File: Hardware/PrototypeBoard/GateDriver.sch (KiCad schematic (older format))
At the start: 38 parts, among them U8 TLE7185-1E

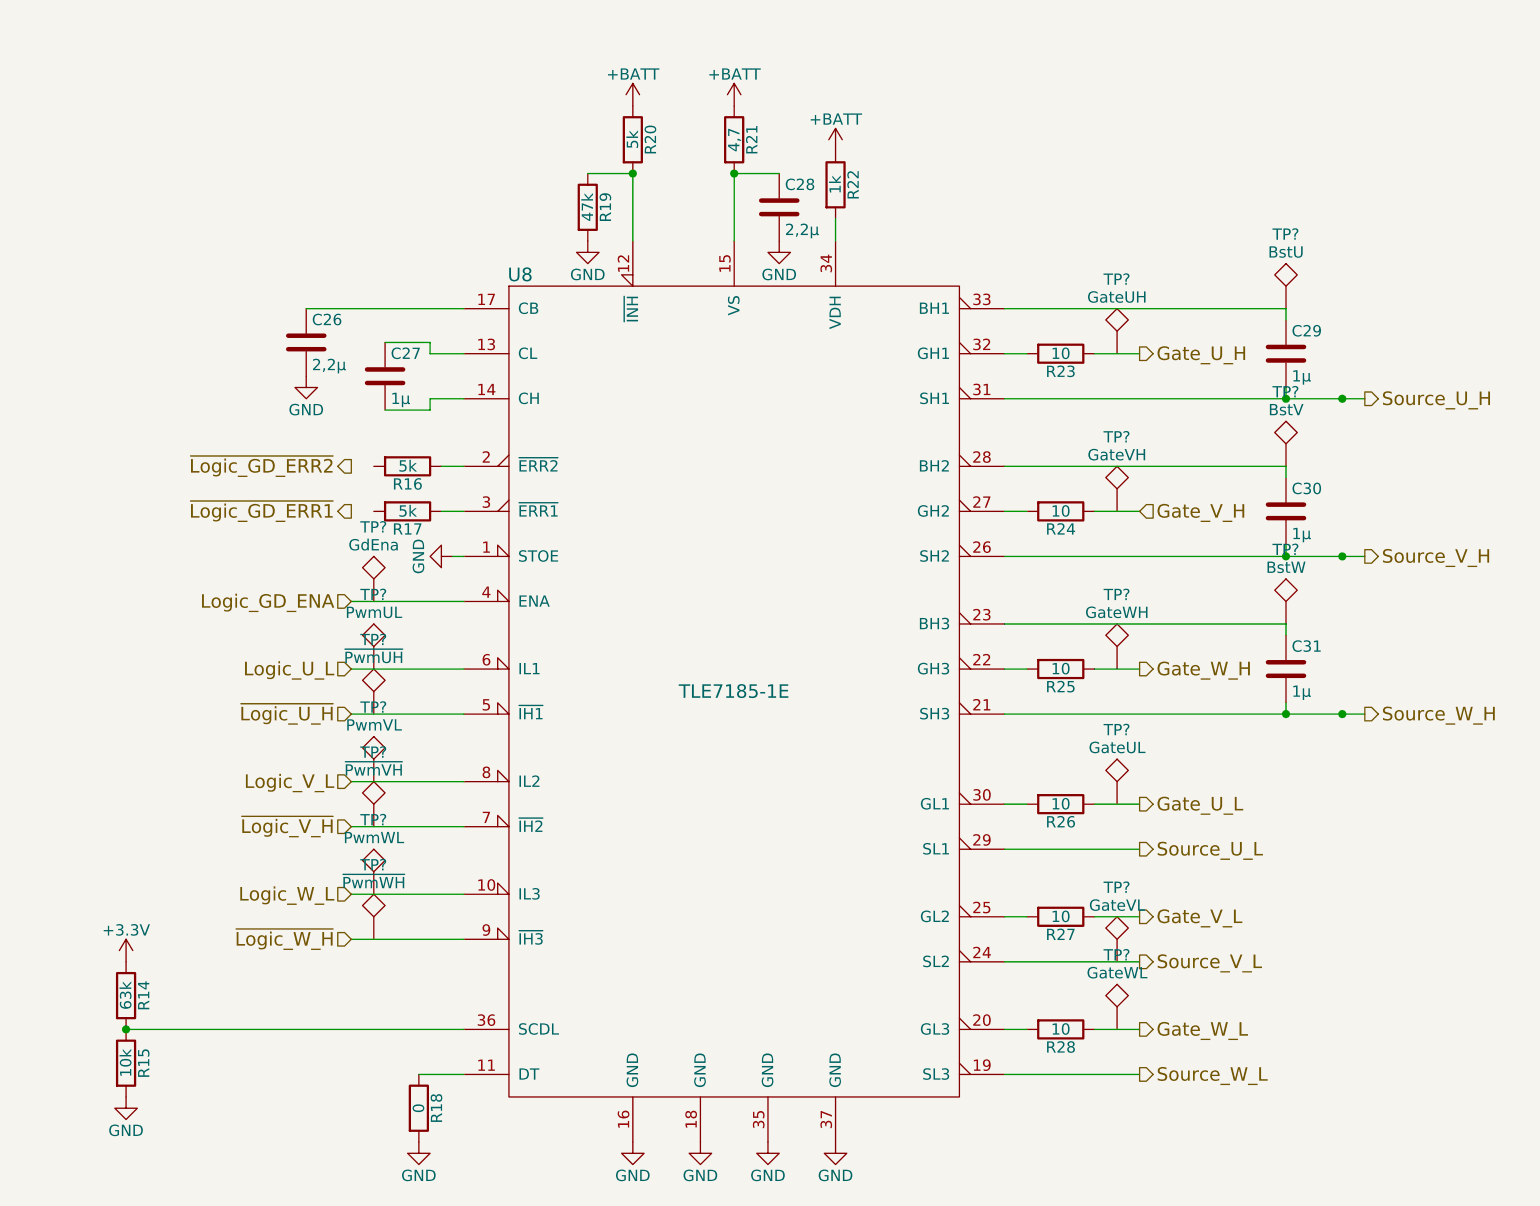
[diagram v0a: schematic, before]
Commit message: Fixed all ERC errors. Added power consumption estimation and other comments. Added links to datasheets. Dimensioned low pass and voltage dividers. Added TVS diodes for protection of voltage rails and ADC inputs. Added fuses. Added Testpoints. Added DC-link capacitors.
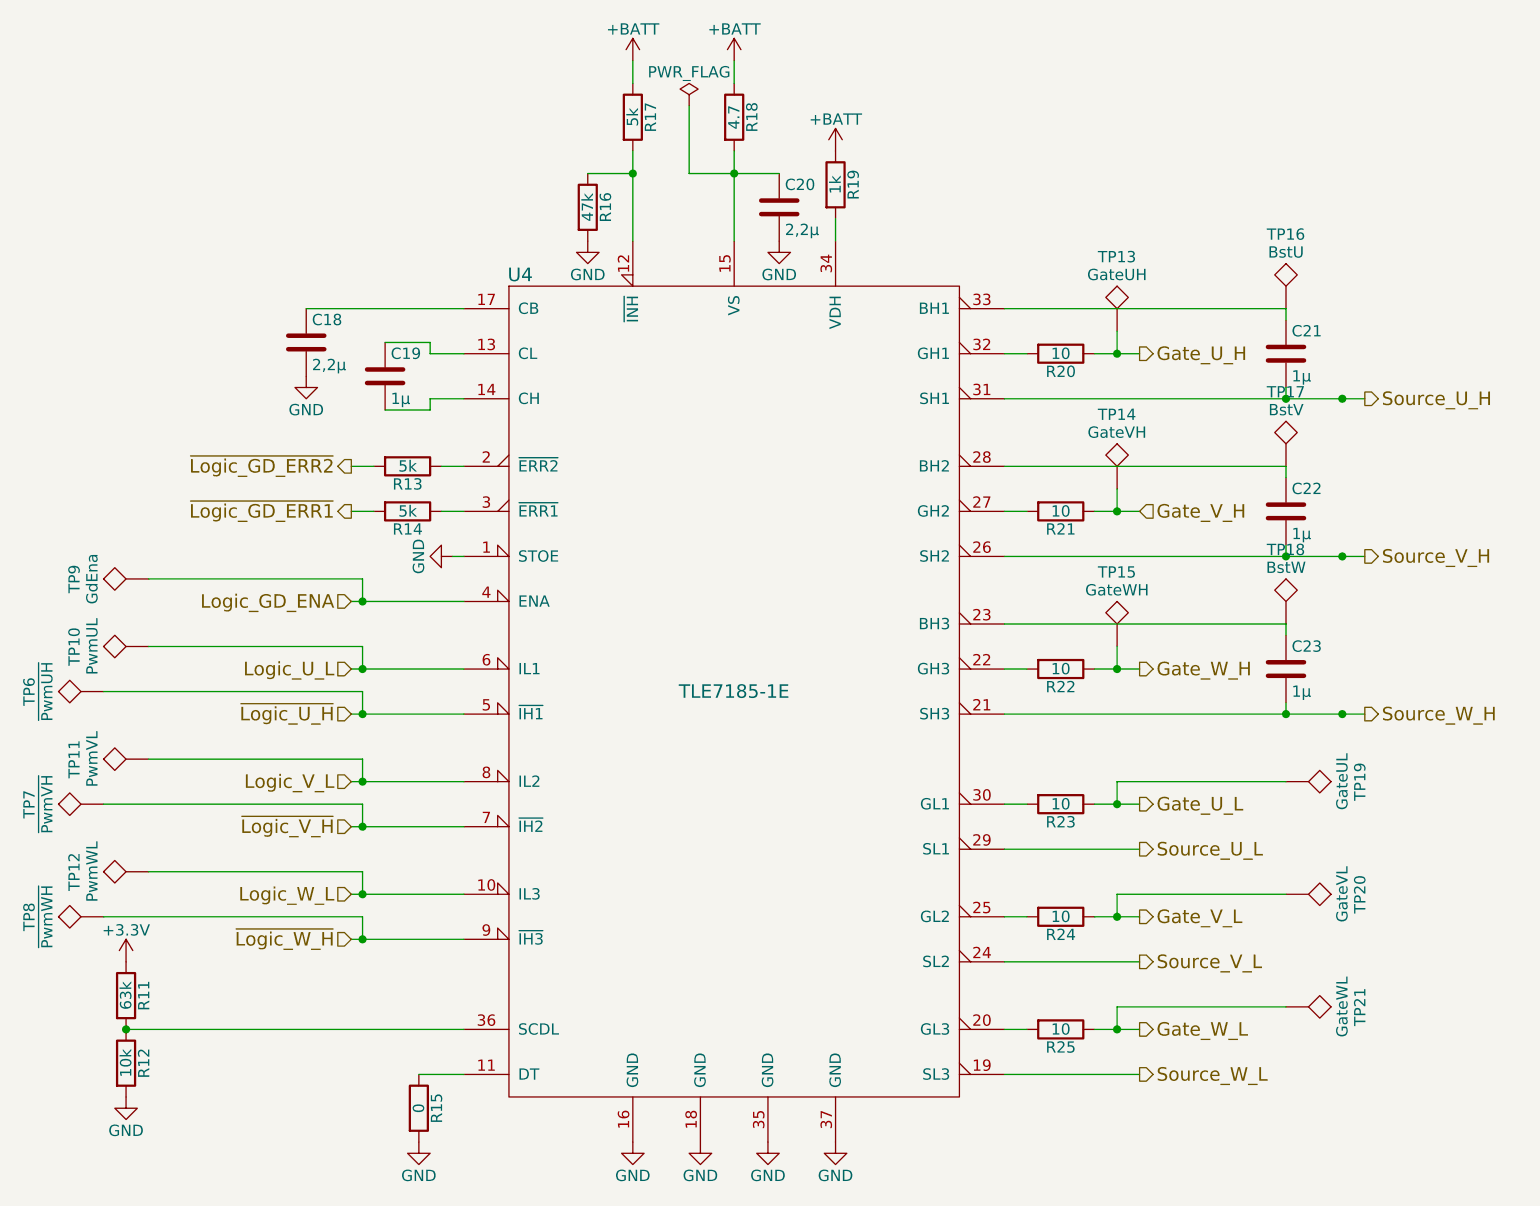
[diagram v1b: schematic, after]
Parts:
- R18: renamed from R21; value 4,7 -> 4.7
- gave numbers to parts that had none: 16
- renumbered C26 to C18, C27 to C19, C28 to C20, C29 to C21, C30 to C22, C31 to C23, R14 to R11, R15 to R12, R16 to R13, R17 to R14, R18 to R15, R19 to R16, R20 to R17, R22 to R19, R23 to R20, R24 to R21, R25 to R22, R26 to R23, R27 to R24, R28 to R25, U8 to U4
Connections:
- net Gate_U_H: now also TP13.1
- net Gate_U_L: now also TP19.1
- net Gate_V_H: now also TP14.1
- net Gate_V_L: now also TP20.1
- net Gate_W_H: now also TP15.1
- net Gate_W_L: now also TP21.1
- net Logic_GD_ENA: now also TP9.1
- net Logic_U_L: now also TP10.1
- net Logic_V_L: now also TP11.1
- net Logic_W_L: now also TP12.1
- net ~Logic_GD_ERR1: now also R14.2
- net ~Logic_GD_ERR2: now also R13.2
- net ~Logic_U_H: now also TP6.1
- net ~Logic_V_H: now also TP7.1
- net ~Logic_W_H: now also TP8.1
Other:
- moved on the sheet: R17, R18, TP10, TP11, TP12, TP13, TP14, TP15, TP19, TP20, TP21, TP6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

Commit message: forgot files
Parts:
- TP10, TP11, TP12, TP13, TP14, TP15, TP16, TP17, TP18, TP19, TP20, TP21, TP6, TP7, TP8, TP9: footprint (none) -> Measurement_Points:Measurement_Point_Round-TH_Big
- U4: footprint (none) -> libs:PG-DSO-36-38
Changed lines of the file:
@@
 F 0 "U4" H 3550 5450 60  0000 C CNN
 F 1 "TLE7185-1E" H 4500 3600 60  0000 C CNN
-F 2 "" H 4500 3600 60  0001 C CNN
+F 2 "libs:PG-DSO-36-38" H 4500 3600 60  0001 C CNN
 F 3 "" H 4500 3600 60  0000 C CNN
 	1    4500 3600
@@
 F 0 "TP17" H 6950 2900 50  0000 C BNN
 F 1 "BstV" H 6950 2850 50  0000 C CNN
-F 2 "" H 6950 2600 50  0001 C CNN
+F 2 "Measurement_Points:Measurement_Point_Round-TH_Big" H 6950 2600 50  0001 C CNN
 F 3 "" H 6950 2600 50  0001 C CNN
 	1    6950 2600
@@
 F 0 "TP16" H 6950 2200 50  0000 C BNN
 F 1 "BstU" H 6950 2150 50  0000 C CNN
-F 2 "" H 6950 1900 50  0001 C CNN
+F 2 "Measurement_Points:Measurement_Point_Round-TH_Big" H 6950 1900 50  0001 C CNN
 F 3 "" H 6950 1900 50  0001 C CNN
 	1    6950 1900
@@
 F 0 "TP18" H 6950 3600 50  0000 C BNN
 F 1 "BstW" H 6950 3550 50  0000 C CNN
-F 2 "" H 6950 3300 50  0001 C CNN
+F 2 "Measurement_Points:Measurement_Point_Round-TH_Big" H 6950 3300 50  0001 C CNN
 F 3 "" H 6950 3300 50  0001 C CNN
 	1    6950 3300
@@
 F 0 "TP14" H 6200 3000 50  0000 C BNN
 F 1 "GateVH" H 6200 2950 50  0000 C CNN
-F 2 "" H 6200 2700 50  0001 C CNN
+F 2 "Measurement_Points:Measurement_Point_Round-TH_Big" H 6200 2700 50  0001 C CNN
 F 3 "" H 6200 2700 50  0001 C CNN
 	1    6200 2700
@@
 F 0 "TP13" H 6200 2300 50  0000 C BNN
 F 1 "GateUH" H 6200 2250 50  0000 C CNN
-F 2 "" H 6200 2000 50  0001 C CNN
+F 2 "Measurement_Points:Measurement_Point_Round-TH_Big" H 6200 2000 50  0001 C CNN
 F 3 "" H 6200 2000 50  0001 C CNN
 	1    6200 2000
@@
 F 0 "TP15" H 6200 3700 50  0000 C BNN
 F 1 "GateWH" H 6200 3650 50  0000 C CNN
-F 2 "" H 6200 3400 50  0001 C CNN
+F 2 "Measurement_Points:Measurement_Point_Round-TH_Big" H 6200 3400 50  0001 C CNN
 F 3 "" H 6200 3400 50  0001 C CNN
 	1    6200 3400
@@
 F 0 "TP19" H 6950 4300 50  0000 C BNN
 F 1 "GateUL" H 6950 4250 50  0000 C CNN
-F 2 "" H 6950 4000 50  0001 C CNN
+F 2 "Measurement_Points:Measurement_Point_Round-TH_Big" H 6950 4000 50  0001 C CNN
 F 3 "" H 6950 4000 50  0001 C CNN
 	1    6950 4000
@@
 F 0 "TP20" H 6950 4800 50  0000 C BNN
 F 1 "GateVL" H 6950 4750 50  0000 C CNN
-F 2 "" H 6950 4500 50  0001 C CNN
+F 2 "Measurement_Points:Measurement_Point_Round-TH_Big" H 6950 4500 50  0001 C CNN
 F 3 "" H 6950 4500 50  0001 C CNN
 	1    6950 4500
@@
 F 0 "TP21" H 6950 5300 50  0000 C BNN
 F 1 "GateWL" H 6950 5250 50  0000 C CNN
-F 2 "" H 6950 5000 50  0001 C CNN
+F 2 "Measurement_Points:Measurement_Point_Round-TH_Big" H 6950 5000 50  0001 C CNN
 F 3 "" H 6950 5000 50  0001 C CNN
 	1    6950 5000
@@
 F 0 "TP9" H 1900 3400 50  0000 C BNN
 F 1 "GdEna" H 1900 3350 50  0000 C CNN
-F 2 "" H 1900 3100 50  0001 C CNN
+F 2 "Measurement_Points:Measurement_Point_Round-TH_Big" H 1900 3100 50  0001 C CNN
 F 3 "" H 1900 3100 50  0001 C CNN
 	1    1900 3100
@@
 F 0 "TP10" H 1900 3700 50  0000 C BNN
 F 1 "PwmUL" H 1900 3650 50  0000 C CNN
-F 2 "" H 1900 3400 50  0001 C CNN
+F 2 "Measurement_Points:Measurement_Point_Round-TH_Big" H 1900 3400 50  0001 C CNN
 F 3 "" H 1900 3400 50  0001 C CNN
 	1    1900 3400
@@
 F 0 "TP6" H 1700 3900 50  0000 C BNN
 F 1 "~PwmUH" H 1700 3850 50  0000 C CNN
-F 2 "" H 1700 3600 50  0001 C CNN
+F 2 "Measurement_Points:Measurement_Point_Round-TH_Big" H 1700 3600 50  0001 C CNN
 F 3 "" H 1700 3600 50  0001 C CNN
 	1    1700 3600
@@
 F 0 "TP11" H 1900 4200 50  0000 C BNN
 F 1 "PwmVL" H 1900 4150 50  0000 C CNN
-F 2 "" H 1900 3900 50  0001 C CNN
+F 2 "Measurement_Points:Measurement_Point_Round-TH_Big" H 1900 3900 50  0001 C CNN
 F 3 "" H 1900 3900 50  0001 C CNN
 	1    1900 3900
@@
 F 0 "TP7" H 1700 4400 50  0000 C BNN
 F 1 "~PwmVH" H 1700 4350 50  0000 C CNN
-F 2 "" H 1700 4100 50  0001 C CNN
+F 2 "Measurement_Points:Measurement_Point_Round-TH_Big" H 1700 4100 50  0001 C CNN
 F 3 "" H 1700 4100 50  0001 C CNN
 	1    1700 4100
@@
 F 0 "TP12" H 1900 4700 50  0000 C BNN
 F 1 "PwmWL" H 1900 4650 50  0000 C CNN
-F 2 "" H 1900 4400 50  0001 C CNN
+F 2 "Measurement_Points:Measurement_Point_Round-TH_Big" H 1900 4400 50  0001 C CNN
 F 3 "" H 1900 4400 50  0001 C CNN
 	1    1900 4400
@@
 F 0 "TP8" H 1700 4900 50  0000 C BNN
 F 1 "~PwmWH" H 1700 4850 50  0000 C CNN
-F 2 "" H 1700 4600 50  0001 C CNN
+F 2 "Measurement_Points:Measurement_Point_Round-TH_Big" H 1700 4600 50  0001 C CNN
 F 3 "" H 1700 4600 50  0001 C CNN
 	1    1700 4600

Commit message: minor progress in layout
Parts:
- TP10, TP11, TP12, TP13, TP14, TP15, TP16, TP17, TP18, TP19, TP20, TP21, TP6, TP7, TP8, TP9: footprint Measurement_Points:Measurement_Point_Round-TH_Big -> Measurement_Points:Measurement_Point_Round-SMD-Pad_Small
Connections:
- net Gate_W_L_bR: now reaches R25.2, U4.20 (GL3)
- net Gate_W_H_bR: now reaches R22.2, U4.22 (GH3)
- net Gate_V_L_bR: now reaches R24.2, U4.25 (GL2)
- net Gate_V_H_bR: now reaches R21.2, U4.27 (GH2)
- net Gate_U_L_bR: now reaches R23.2, U4.30 (GL1)
- net Gate_U_H_bR: now reaches R20.2, U4.32 (GH1)
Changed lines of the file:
@@
 F 0 "TP17" H 6950 2900 50  0000 C BNN
 F 1 "BstV" H 6950 2850 50  0000 C CNN
-F 2 "Measurement_Points:Measurement_Point_Round-TH_Big" H 6950 2600 50  0001 C CNN
+F 2 "Measurement_Points:Measurement_Point_Round-SMD-Pad_Small" H 6950 2600 50  0001 C CNN
 F 3 "" H 6950 2600 50  0001 C CNN
 	1    6950 2600
@@
 F 0 "TP16" H 6950 2200 50  0000 C BNN
 F 1 "BstU" H 6950 2150 50  0000 C CNN
-F 2 "Measurement_Points:Measurement_Point_Round-TH_Big" H 6950 1900 50  0001 C CNN
+F 2 "Measurement_Points:Measurement_Point_Round-SMD-Pad_Small" H 6950 1900 50  0001 C CNN
 F 3 "" H 6950 1900 50  0001 C CNN
 	1    6950 1900
@@
 F 0 "TP18" H 6950 3600 50  0000 C BNN
 F 1 "BstW" H 6950 3550 50  0000 C CNN
-F 2 "Measurement_Points:Measurement_Point_Round-TH_Big" H 6950 3300 50  0001 C CNN
+F 2 "Measurement_Points:Measurement_Point_Round-SMD-Pad_Small" H 6950 3300 50  0001 C CNN
 F 3 "" H 6950 3300 50  0001 C CNN
 	1    6950 3300
@@
 F 0 "TP14" H 6200 3000 50  0000 C BNN
 F 1 "GateVH" H 6200 2950 50  0000 C CNN
-F 2 "Measurement_Points:Measurement_Point_Round-TH_Big" H 6200 2700 50  0001 C CNN
+F 2 "Measurement_Points:Measurement_Point_Round-SMD-Pad_Small" H 6200 2700 50  0001 C CNN
 F 3 "" H 6200 2700 50  0001 C CNN
 	1    6200 2700
@@
 F 0 "TP13" H 6200 2300 50  0000 C BNN
 F 1 "GateUH" H 6200 2250 50  0000 C CNN
-F 2 "Measurement_Points:Measurement_Point_Round-TH_Big" H 6200 2000 50  0001 C CNN
+F 2 "Measurement_Points:Measurement_Point_Round-SMD-Pad_Small" H 6200 2000 50  0001 C CNN
 F 3 "" H 6200 2000 50  0001 C CNN
 	1    6200 2000
@@
 F 0 "TP15" H 6200 3700 50  0000 C BNN
 F 1 "GateWH" H 6200 3650 50  0000 C CNN
-F 2 "Measurement_Points:Measurement_Point_Round-TH_Big" H 6200 3400 50  0001 C CNN
+F 2 "Measurement_Points:Measurement_Point_Round-SMD-Pad_Small" H 6200 3400 50  0001 C CNN
 F 3 "" H 6200 3400 50  0001 C CNN
 	1    6200 3400
@@
 F 0 "TP19" H 6950 4300 50  0000 C BNN
 F 1 "GateUL" H 6950 4250 50  0000 C CNN
-F 2 "Measurement_Points:Measurement_Point_Round-TH_Big" H 6950 4000 50  0001 C CNN
+F 2 "Measurement_Points:Measurement_Point_Round-SMD-Pad_Small" H 6950 4000 50  0001 C CNN
 F 3 "" H 6950 4000 50  0001 C CNN
 	1    6950 4000
@@
 F 0 "TP20" H 6950 4800 50  0000 C BNN
 F 1 "GateVL" H 6950 4750 50  0000 C CNN
-F 2 "Measurement_Points:Measurement_Point_Round-TH_Big" H 6950 4500 50  0001 C CNN
+F 2 "Measurement_Points:Measurement_Point_Round-SMD-Pad_Small" H 6950 4500 50  0001 C CNN
 F 3 "" H 6950 4500 50  0001 C CNN
 	1    6950 4500
@@
 F 0 "TP21" H 6950 5300 50  0000 C BNN
 F 1 "GateWL" H 6950 5250 50  0000 C CNN
-F 2 "Measurement_Points:Measurement_Point_Round-TH_Big" H 6950 5000 50  0001 C CNN
+F 2 "Measurement_Points:Measurement_Point_Round-SMD-Pad_Small" H 6950 5000 50  0001 C CNN
 F 3 "" H 6950 5000 50  0001 C CNN
 	1    6950 5000
@@
 F 0 "TP9" H 1900 3400 50  0000 C BNN
 F 1 "GdEna" H 1900 3350 50  0000 C CNN
-F 2 "Measurement_Points:Measurement_Point_Round-TH_Big" H 1900 3100 50  0001 C CNN
+F 2 "Measurement_Points:Measurement_Point_Round-SMD-Pad_Small" H 1900 3100 50  0001 C CNN
 F 3 "" H 1900 3100 50  0001 C CNN
 	1    1900 3100
@@
 F 0 "TP10" H 1900 3700 50  0000 C BNN
 F 1 "PwmUL" H 1900 3650 50  0000 C CNN
-F 2 "Measurement_Points:Measurement_Point_Round-TH_Big" H 1900 3400 50  0001 C CNN
+F 2 "Measurement_Points:Measurement_Point_Round-SMD-Pad_Small" H 1900 3400 50  0001 C CNN
 F 3 "" H 1900 3400 50  0001 C CNN
 	1    1900 3400
@@
 F 0 "TP6" H 1700 3900 50  0000 C BNN
 F 1 "~PwmUH" H 1700 3850 50  0000 C CNN
-F 2 "Measurement_Points:Measurement_Point_Round-TH_Big" H 1700 3600 50  0001 C CNN
+F 2 "Measurement_Points:Measurement_Point_Round-SMD-Pad_Small" H 1700 3600 50  0001 C CNN
 F 3 "" H 1700 3600 50  0001 C CNN
 	1    1700 3600
@@
 F 0 "TP11" H 1900 4200 50  0000 C BNN
 F 1 "PwmVL" H 1900 4150 50  0000 C CNN
-F 2 "Measurement_Points:Measurement_Point_Round-TH_Big" H 1900 3900 50  0001 C CNN
+F 2 "Measurement_Points:Measurement_Point_Round-SMD-Pad_Small" H 1900 3900 50  0001 C CNN
 F 3 "" H 1900 3900 50  0001 C CNN
 	1    1900 3900
@@
 F 0 "TP7" H 1700 4400 50  0000 C BNN
 F 1 "~PwmVH" H 1700 4350 50  0000 C CNN
-F 2 "Measurement_Points:Measurement_Point_Round-TH_Big" H 1700 4100 50  0001 C CNN
+F 2 "Measurement_Points:Measurement_Point_Round-SMD-Pad_Small" H 1700 4100 50  0001 C CNN
 F 3 "" H 1700 4100 50  0001 C CNN
 	1    1700 4100
@@
 F 0 "TP12" H 1900 4700 50  0000 C BNN
 F 1 "PwmWL" H 1900 4650 50  0000 C CNN
-F 2 "Measurement_Points:Measurement_Point_Round-TH_Big" H 1900 4400 50  0001 C CNN
+F 2 "Measurement_Points:Measurement_Point_Round-SMD-Pad_Small" H 1900 4400 50  0001 C CNN
 F 3 "" H 1900 4400 50  0001 C CNN
 	1    1900 4400
@@
 F 0 "TP8" H 1700 4900 50  0000 C BNN
 F 1 "~PwmWH" H 1700 4850 50  0000 C CNN
-F 2 "Measurement_Points:Measurement_Point_Round-TH_Big" H 1700 4600 50  0001 C CNN
+F 2 "Measurement_Points:Measurement_Point_Round-SMD-Pad_Small" H 1700 4600 50  0001 C CNN
 F 3 "" H 1700 4600 50  0001 C CNN
 	1    1700 4600
@@
 Wire Wire Line
 	4300 1000 4300 1300
+Text Label 5750 2100 0    60   ~ 0
+Gate_U_H_bR
+Text Label 5750 2800 0    60   ~ 0
+Gate_V_H_bR
+Text Label 5750 3500 0    60   ~ 0
+Gate_W_H_bR
+Text Label 5750 4100 0    60   ~ 0
+Gate_U_L_bR
+Text Label 5750 4600 0    60   ~ 0
+Gate_V_L_bR
+Text Label 5750 5100 0    60   ~ 0
+Gate_W_L_bR
 $EndSCHEMATC

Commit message: some more layout...
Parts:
- renumbered C18 to C21, C19 to C22, C20 to C23, C21 to C24, C22 to C25, C23 to C26
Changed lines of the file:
@@
 ~Logic_GD_ERR2
 $Comp
-L C C19
+L C C22
 U 1 1 56C25879
 P 2950 2200
-F 0 "C19" H 2975 2300 50  0000 L CNN
+F 0 "C22" H 2975 2300 50  0000 L CNN
 F 1 "1µ" H 2975 2100 50  0000 L CNN
 F 2 "Capacitors_SMD:C_0805_HandSoldering" H 2988 2050 50  0001 C CNN
@@
 	3150 2350 2950 2350
 $Comp
-L C C18
+L C C21
 U 1 1 56C25915
 P 2600 2050
-F 0 "C18" H 2625 2150 50  0000 L CNN
+F 0 "C21" H 2625 2150 50  0000 L CNN
 F 1 "2,2µ" H 2625 1950 50  0000 L CNN
 F 2 "Capacitors_SMD:C_0805_HandSoldering" H 2638 1900 50  0001 C CNN
@@
 $EndComp
 $Comp
-L C C20
+L C C23
 U 1 1 56C25EA2
 P 4700 1450
-F 0 "C20" H 4725 1550 50  0000 L CNN
+F 0 "C23" H 4725 1550 50  0000 L CNN
 F 1 "2,2µ" H 4725 1350 50  0000 L CNN
 F 2 "Capacitors_SMD:C_0805_HandSoldering" H 4738 1300 50  0001 C CNN
@@
 Source_W_H
 $Comp
-L C C21
+L C C24
 U 1 1 56C26607
 P 6950 2100
-F 0 "C21" H 6975 2200 50  0000 L CNN
+F 0 "C24" H 6975 2200 50  0000 L CNN
 F 1 "1µ" H 6975 2000 50  0000 L CNN
 F 2 "Capacitors_SMD:C_0805_HandSoldering" H 6988 1950 50  0001 C CNN
@@
 $EndComp
 $Comp
-L C C22
+L C C25
 U 1 1 56C266D2
 P 6950 2800
-F 0 "C22" H 6975 2900 50  0000 L CNN
+F 0 "C25" H 6975 2900 50  0000 L CNN
 F 1 "1µ" H 6975 2700 50  0000 L CNN
 F 2 "Capacitors_SMD:C_0805_HandSoldering" H 6988 2650 50  0001 C CNN
@@
 $EndComp
 $Comp
-L C C23
+L C C26
 U 1 1 56C26727
 P 6950 3500
-F 0 "C23" H 6975 3600 50  0000 L CNN
+F 0 "C26" H 6975 3600 50  0000 L CNN
 F 1 "1µ" H 6975 3400 50  0000 L CNN
 F 2 "Capacitors_SMD:C_0805_HandSoldering" H 6988 3350 50  0001 C CNN
